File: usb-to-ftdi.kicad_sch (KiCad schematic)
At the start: 11 parts, among them J1 USB_OTG, J2 Conn_01x06, Q1 BSS138, Q2 BSS138, U1 AMS1117-3.3, U2 CH340C

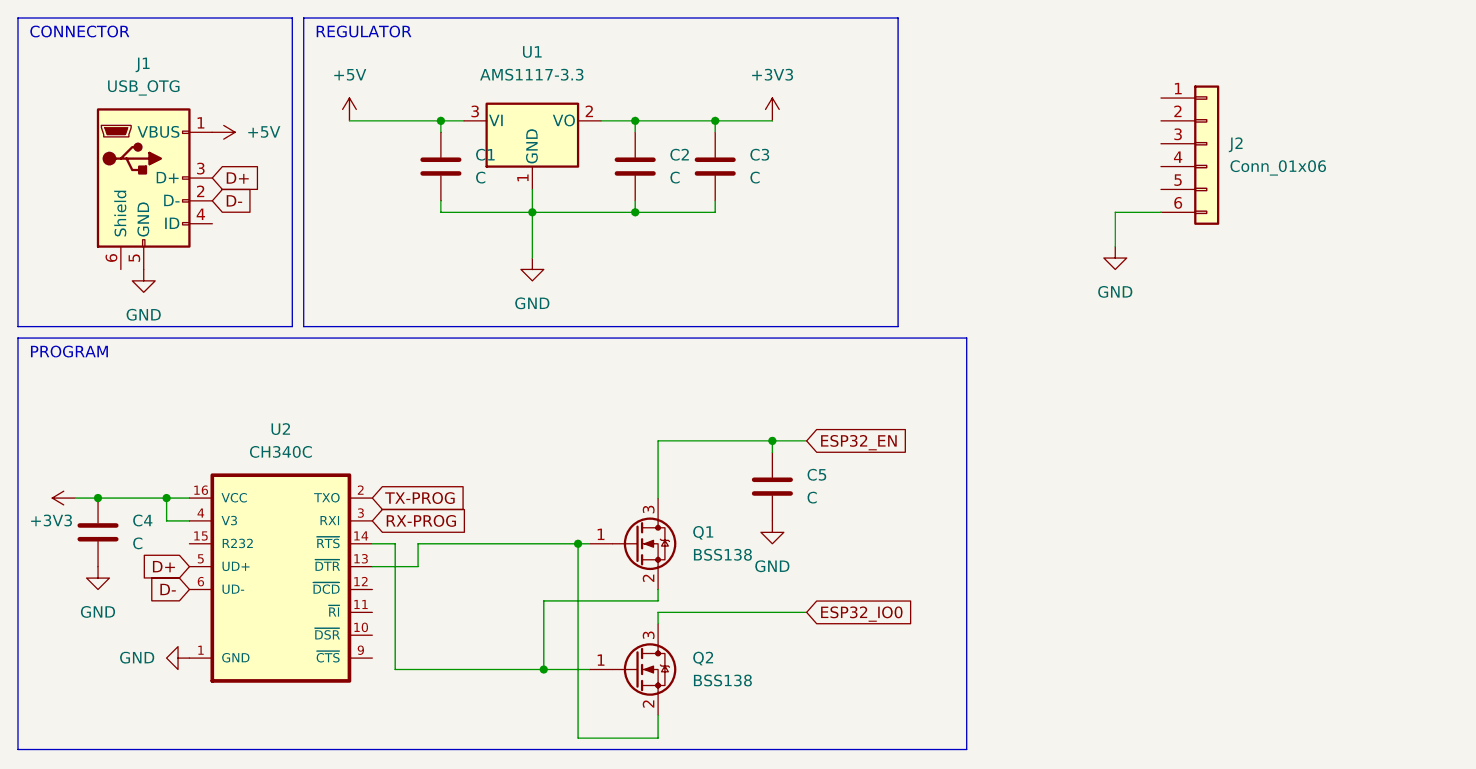
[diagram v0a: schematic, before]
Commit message: update wiring + add jumper vcc
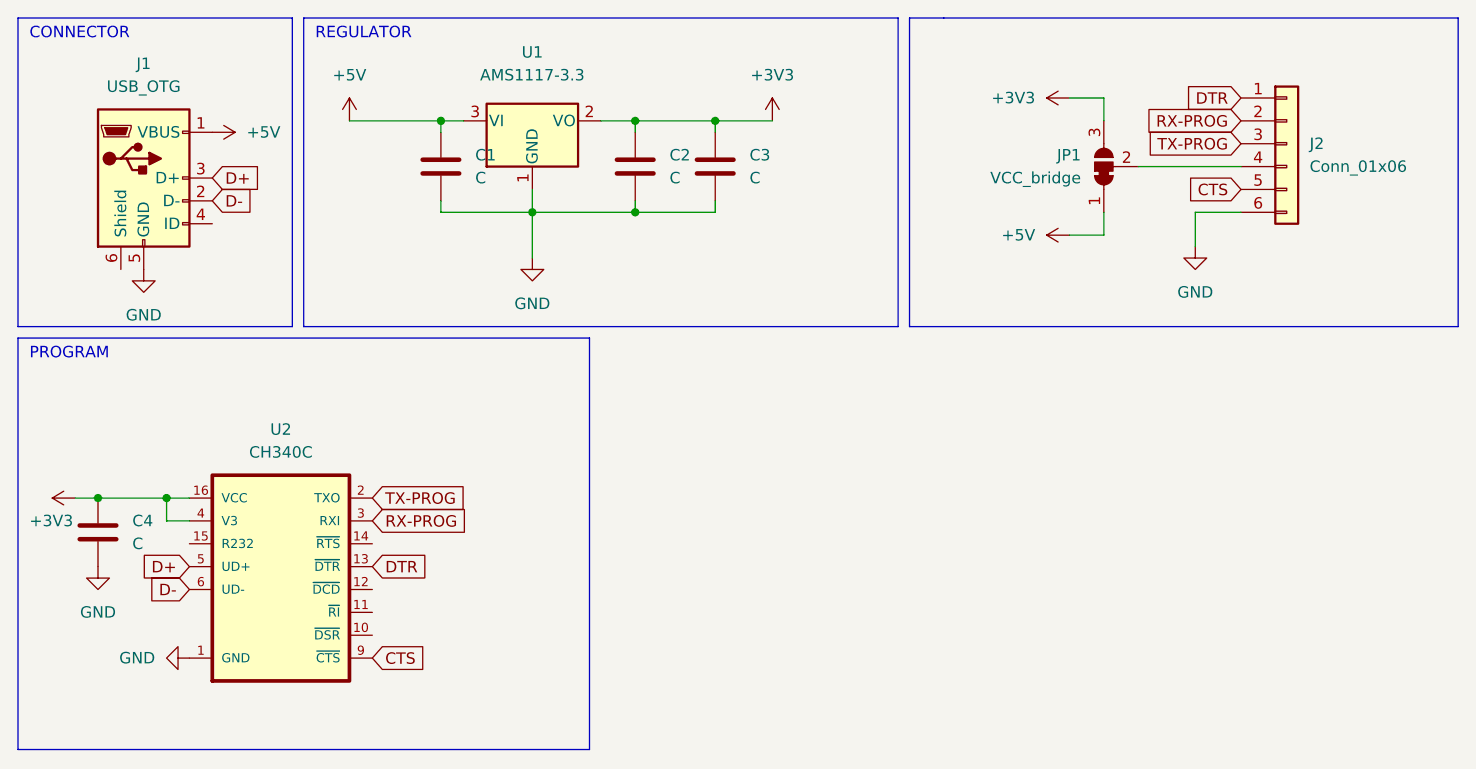
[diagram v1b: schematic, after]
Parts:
- removed C5: C, Capacitor_SMD:C_0603_1608Metric, symbol Device:C
- removed Q1, Q2: BSS138, Package_TO_SOT_SMD:SOT-23, symbol Transistor_FET:BSS138
- added JP1: VCC_bridge, symbol Jumper:SolderJumper_3_Bridged12
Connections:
- net +3V3: now also JP1.3 (B)
- net +5V: now also JP1.1 (A)
- net RX-PROG: now also J2.2 (Pin_2)
- net TX-PROG: now also J2.3 (Pin_3)
- net DTR: now reaches U2.13 (~{DTR})
- net DTR: now also J2.1 (Pin_1)
- net CTS: now reaches U2.9 (~{CTS})
- net CTS: now also J2.5 (Pin_5)
- net at J2.4 (Pin_4): now also JP1.2 (C)
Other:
- moved on the sheet: J2

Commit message: add pcb + wiring
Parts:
- removed U2: CH340C, CH340C:SO016, symbol CH340C:CH340C
- added U3: CH340C, CH340C:SOIC127P600X180-16N, symbol CH340:CH340C
- J2: footprint (none) -> Connector_PinHeader_2.54mm:PinHeader_1x06_P2.54mm_Vertical
- JP1: footprint (none) -> Jumper:SolderJumper-3_P1.3mm_Bridged12_Pad1.0x1.5mm
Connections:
- net +3V3: now also U3.16 (VCC), U3.4 (V3)
- net CTS: now also U3.9 (~{CTS})
- net D+: now also U3.5 (UD+)
- net D-: now also U3.6 (UD-)
- net DTR: now also U3.13 (~{DTR})
- net RX-PROG: now also U3.3 (RXD)
- net TX-PROG: now also U3.2 (TXD)
